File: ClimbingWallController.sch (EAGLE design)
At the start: 336 parts, among them IC1 74HCT138D, IC2 74HCT138D, IC3 PIC24FJ32GB004, IC4 SN74LV4052AD, IC5 SN74LV4052AD, IC6 TC1015, IC7 NCP1117, J1 PWR, Q1 DPBT8105, Q10 DPBT8105, Q11 DPBT8105, Q12 DPBT8105, Q13 DPBT8105, Q14 DPBT8105, Q15 DPBT8105, Q16 DPBT8105, Q17 NC, Q2 DPBT8105, Q3 DPBT8105, Q4 DPBT8105, Q5 DPBT8105, Q6 DPBT8105, Q7 DPBT8105, Q8 DPBT8105, Q9 DPBT8105, X1 MINI-USB-32005-201

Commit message: Completed routing of all circuit board elements. Created ground fills, and stitched everything together. Need to review sensitive signal coupling and review decoupling paths. Need to verify footprints.
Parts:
- added C100, C101, C99: 0.1uF, rcl:C-USC0603K
- JP1: device pinhead:PINHD-1X5/90 -> pinhead:PINHD-1X5
- XTAL1: device crystal:CRYSTALHC49UP -> Parts:CRY5032
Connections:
- removed net N$86: R85.1, R86.2
- net +5V: now also C100.1, C101.1, C99.1
- net GND: now also C100.2, C101.2, C99.2
- net TMUX0: now also IC3.AN10; no longer IC3.AN11
- net TMUX1: now also IC3.AN11; no longer IC3.AN10
- net TOUCH11: now also IC3.AN12; no longer IC5.Y0
- net TOUCH12: now also IC3.AN8; no longer IC5.Y1
- net TOUCH13: now also IC3.AN7; no longer IC5.Y2
- net TOUCH14: now also IC5.Y2; no longer IC5.Y3
- net TOUCH15: now also IC5.Y0; no longer IC5.X0
- net TOUCH16: now also IC5.Y3; no longer IC5.X1
- net TOUCH17: now also IC5.Y1; no longer IC5.X2
- net TOUCH18: now also IC5.X2; no longer IC5.X3
- net TOUCH19: now also IC5.X1; no longer IC3.AN7
- net TOUCH20: now also IC5.X0; no longer IC3.AN8
- net TOUCH21: now also IC5.X3; no longer IC3.AN12
- net VREF+: now also R85.1, R86.2

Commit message: Cleaned up floating ratsnest wires. Cleaned up DRC Errors. Need to check DRC with SEEED's rule set.
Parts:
- IC8, IC9: value TLC5952 -> (none)
- R1, R10, R100, R101, R102, R103, R104, R105, R106, R107, R108, R109, R11, R110, R111, R112, R113, R114, R115, R116, R117, R118, R119, R12, R120, R121, R122, R123, R124, R125, R126, R127, R128, R129, R13, R130, R131, R132, R133, R134, R135, R14, R15, R16, R17, R18, R19, R2, R20, R21, R22, R23, R24, R25, R26, R27, R28, R29, R3, R30, R31, R32, R33, R34, R35, R36, R37, R38, R39, R4, R40, R41, R42, R43, R44, R45, R46, R47, R48, R49, R5, R50, R51, R52, R53, R54, R57, R58, R59, R6, R60, R61, R62, R63, R64, R65, R66, R67, R68, R69, R7, R70, R71, R72, R73, R74, R75, R76, R77, R78, R79, R8, R80, R81, R82, R83, R85, R86, R87, R88, R89, R9, R90, R91, R92, R93, R94, R95, R96, R97, R98, R99: device resistor:R-US_R0603 -> Parts:R-US_R0603
- renumbered U$1 to IC8, U$2 to IC9

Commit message: DRC Passed with SEEED Rules. Added extra input to touch connector because 11-socket parts aren't available. Fixed 5v regulator pin out, and added PCB heat sink. Messed with device attributes for manufacturer part number. Exported BOM. (Awaiting clean up for BOM commit).
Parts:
- removed LED0: (no value), Parts:OSTVN12A150
- added LED4: (no value), Parts:OSTVN12A150
- C1: value 22n -> 100uF; device resistor:C-USC0603 -> resistor:CPOL-USD
- C10, C3, C4, C5, C6, C7, C8, C9: device resistor:C-USC0603 -> resistor:C-USC0603K
- C100, C101, C99: value 0.1uF -> 22n; device rcl:C-USC0603K -> resistor:C-USC0603K
- C11, C12, C13, C14: value 22n -> 0.1uF; device resistor:C-USC0603 -> rcl:C-USC0603K
- C15: value 22n -> NC; device resistor:C-USC0603 -> rcl:C-USC0603K
- C16, C90: value NC -> 0.1uF
- C17: value 0.1uF -> NC
- C18, C19, C26, C27, C28, C29, C31: value 0.1uF -> 1n; device rcl:C-USC0603K -> resistor:C-USC0603K
- C2: value 22n -> 1uF; device resistor:C-USC0603 -> rcl:C-USC0603K
- C20: value 22n -> 1n; device resistor:C-USC0603 -> resistor:C-USC0603K
- C21, C22: value NC -> 1n; device rcl:C-USC0603K -> resistor:C-USC0603K
- C23: value 470pF -> 1n; device rcl:C-USC0603K -> resistor:C-USC0603K
- C24: value 10uF -> 0.1uF; device rcl:C-USC1206K -> rcl:C-USC0603K
- C25: value 1uF -> NC
- C30, C39: value 1uF -> 1n; device rcl:C-USC0603K -> resistor:C-USC0603K
- C34: value 100uF -> 1uF; device resistor:CPOL-USD -> rcl:C-USC0603K
- C35: value 100uF -> 0.1uF; device resistor:CPOL-USD -> rcl:C-USC0603K
- C36: value 1uF -> 0.1uF
- C37: value 100uF -> NC; device resistor:CPOL-USD -> rcl:C-USC0603K
- C38: value 10uF -> 1n; device rcl:C-USC1206K -> resistor:C-USC0603K
- C40: value 100uF -> 1n; device resistor:CPOL-USD -> resistor:C-USC0603K
- C50, C51, C53, C55, C68, C70: value 1n -> NC; device resistor:C-USC0603K -> rcl:C-USC0603K
- C52, C72: value 1n -> 10uF; device resistor:C-USC0603K -> rcl:C-USC1206K
- C54, C69, C88: value 1n -> 0.1uF; device resistor:C-USC0603K -> rcl:C-USC0603K
- C71: value 1n -> 1uF; device resistor:C-USC0603K -> rcl:C-USC0603K
- C73: value 1n -> 470pF; device resistor:C-USC0603K -> rcl:C-USC0603K
- C86, C87: value 1n -> 100uF; device resistor:C-USC0603K -> resistor:CPOL-USD
- C92: value NC -> 100uF; device rcl:C-USC0603K -> resistor:CPOL-USD
- C93: value 0.1uF -> 1uF
- C94, C95, C96, C97, C98: value NC -> 22n; device rcl:C-USC0603K -> resistor:C-USC0603K
- IC2: value 74HCT138D -> SN74LV4052AD; device Parts:74HCT138D -> Parts:SN74LV4052AD
- IC4, IC5: value SN74LV4052AD -> TLC5952; device Parts:SN74LV4052AD -> Parts:TLC5952
- IC7: value NCP1117 -> (none)
- IC8: value (none) -> 74HCT138D; device Parts:TLC5952 -> Parts:74HCT138D
- IC9: value (none) -> SN74LV4052AD; device Parts:TLC5952 -> Parts:SN74LV4052AD
- J1: device con-jack:DCJ0303 -> Parts:DCJ0303
- JP1: value DEBUG -> BUZZER; device pinhead:PINHD-1X5 -> pinhead:PINHD-1X2
- JP2: value BUZZER -> DEBUG; device pinhead:PINHD-1X2 -> pinhead:PINHD-1X5
- Q17: value NC -> DPBT8105; device transistor:-NPN-SOT23-EBC -> Parts:DPBT8105
- Q9: value DPBT8105 -> NC; device Parts:DPBT8105 -> transistor:-NPN-SOT23-EBC
- R1, R13, R19, R7: value 20 -> NC
- R10, R22: value 20 -> 750
- R100, R101, R102, R103, R104, R105, R109, R110, R111, R91, R98: value 300 -> 390
- R106, R107, R108: value 300 -> 4.7k
- R112, R114, R116, R118, R124, R126, R128, R130: value 300 -> NC
- R113, R115, R117, R119, R125, R127, R129, R131: value 300 -> 20
- R12, R21, R24, R9: value NC -> 750
- R120, R121, R122, R123, R132, R133, R134, R135: value 300 -> 750
- R14, R2, R20, R8: value 750 -> 20
- R17, R5: value 750 -> NC
- R18, R6: value NC -> 20
- R25, R28, R31, R37: value 20 -> 390
- R26, R29, R32, R44: value 750 -> 390
- R27, R30, R36: value NC -> 390
- R33: value NC -> 4.7k
- R34: value 20 -> 4.7k
- R35: value 750 -> 4.7k
- R38, R41, R47: value 750 -> 300
- R39, R42, R45, R48, R85, R86, R87: value NC -> 300
- R40, R43, R46: value 20 -> 300
- R49, R50, R53, R54, R57, R58, R59, R60: value 4.7k -> 300
- R55, R56: value 1.37k 0.5% -> 300; device resistor:R-US_R0805 -> Parts:R-US_R0603
- R61, R62, R63, R64, R68, R69, R70, R71, R72, R73, R74, R75, R76, R77, R78, R79: value 390 -> 300
- R65, R66: value 390 -> 1.37k 0.5%; device Parts:R-US_R0603 -> resistor:R-US_R0805; TOLERANCE (none) -> 0.5%
- R67, R80: value 390 -> 4.7k
- R81, R83: value 390 -> NC
- R84: value 0 -> NC; device resistor:R-US_R0805 -> Parts:R-US_R0603
- R99: value 300 -> 0; device Parts:R-US_R0603 -> resistor:R-US_R0805
- TCH0, TCH1: device Parts:OSTVN11A150 -> Parts:OSTVN12A150
- X1: MPN (none) -> USB-M26FTR
- XTAL1: MPN (none) -> 7A-12.000MAAJ-T
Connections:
- removed net N$118 (its old number): C67.1, R114.1
- removed net N$66: R65.2, TCH0-4.KL
- removed net N$68: R67.2, TCH0-6.KL
- removed net N$70: R69.2, TCH0-8.KL
- removed net N$72: R71.2, TCH0-10.KL
- removed net N$74: R74.2, TCH1-2.KL
- removed net N$75: R76.2, TCH1-4.KL
- removed net N$76: R78.2, TCH1-6.KL
- removed net N$77: R80.2, TCH1-8.KL
- removed net N$78: R82.2, TCH1-10.KL
- new net N$31: R98.2, TCH0-2.KL
- new net N$32: R101.2, TCH0-4.KL
- new net N$34: C101.1, R131.1
- new net N$35: R103.2, TCH0-6.KL
- new net N$36: R105.2, TCH0-8.KL
- new net N$37: R110.2, TCH0-10.KL
- new net N$38: R26.2, TCH1-2.KL
- new net N$39: R28.2, TCH1-4.KL
- new net N$40: R30.2, TCH1-6.KL
- new net N$49: R37.2, TCH1-10.KL
- net +3V3: now also C14.1, C15.1, C25.1, C34.1, C35.1, C36.1, C37.1, C54.1, C55.1, C69.1, C70.1, C72.1, C88.1, IC2.VCC, JP2.2, R80.2, R81.2; no longer C17.1, C18.1, C19.1, C26.1, C27.1, C30.1, C31.1, C90.1, C91.1, C93.1, C94.1, C95.1, C98.1, IC8.VCC, JP1.2, R60.2, R85.2
- net +5V: now also C1.+, C11.1, C12.1, C13.1, C16.1, C17.1, C2.1, C71.1, C87.+, C90.1, C91.1, C92.+, C93.1, D10.C, D11.C, D12.C, D13.C, D14.C, D15.C, D16.C, D9.C, IC7.OUT, IC8.VCC, JP1.1, Q17.E, R1.1, R112.1, R114.1, R116.1, R118.1, R124.1, R126.1, R128.1, R13.1, R130.1, R17.1, R19.1, R5.1, R7.1, R99.2; no longer C100.1, C101.1, C25.1, C28.1, C29.1, C34.+, C36.1, C37.+, C39.1, C40.+, C96.1, C97.1, C99.1, D57.C, D58.C, D59.C, D60.C, D61.C, D62.C, D63.C, D64.C, IC2.VCC, IC7G$1.OUT, JP2.1, Q9.E, R12.1, R18.1, R21.1, R24.1, R27.1, R30.1, R33.1, R36.1, R39.1, R42.1, R45.1, R48.1, R6.1, R84.2, R9.1
- net AMSEL0: now also IC2.A, IC9.A; no longer IC4.A, IC5.A
- net AMSEL1: now also IC2.B, IC9.B; no longer IC4.B, IC5.B
- net B0: now also D17.A, IC5.OUTB0, LED2-3.KL, R47.2; no longer D19.A, IC8.OUTB0, LED0-3.KL, R90.2
- net B1: now also D20.A, IC5.OUTB1, LED2-6.KL, R50.2; no longer D22.A, IC8.OUTB1, LED0-6.KL, R93.2
- net B10: now also D23.A, IC4.OUTB2, LED1-9.KL, R55.2; no longer D49.A, IC9.OUTB2, LED2-9.KL, R120.2
- net B11: now also D26.A, IC4.OUTB3, LED1-12.KL, R58.2; no longer D52.A, IC9.OUTB3, LED2-12.KL, R123.2
- net B12: now also D35.A, IC4.OUTB4, R70.2; no longer D55.A, IC9.OUTB4, R126.2
- net B13: now also D38.A, IC4.OUTB5, R73.2; no longer D58.A, IC9.OUTB5, R129.2
- net B14: now also D47.A, IC4.OUTB6, R87.2; no longer D61.A, IC9.OUTB6, R132.2
- net B15: now also D50.A, IC4.OUTB7, R90.2; no longer D64.A, IC9.OUTB7, R135.2
- net B2: now also D29.A, IC5.OUTB2, LED2-9.KL, R61.2; no longer D25.A, IC8.OUTB2, LED0-9.KL, R96.2
- net B3: now also D32.A, IC5.OUTB3, LED2-12.KL, R64.2; no longer D28.A, IC8.OUTB3, LED0-12.KL, R99.2
- net B4: now also D41.A, IC5.OUTB4, LED4-3.KL, R76.2; no longer D31.A, IC8.OUTB4, LED1-3.KL, R102.2
- net B5: now also D44.A, IC5.OUTB5, LED4-6.KL, R79.2; no longer D34.A, IC8.OUTB5, LED1-6.KL, R105.2
- net B6: now also D53.A, IC5.OUTB6, LED4-9.KL, R94.2; no longer D37.A, IC8.OUTB6, LED1-9.KL, R108.2
- net B7: now also D56.A, IC5.OUTB7, LED4-12.KL, R97.2; no longer D40.A, IC8.OUTB7, LED1-12.KL, R111.2
- net B8: now also D11.A, IC4.OUTB0, LED1-3.KL, R40.2; no longer D43.A, IC9.OUTB0, LED2-3.KL, R114.2
- net B9: now also D14.A, IC4.OUTB1, LED1-6.KL, R43.2; no longer D46.A, IC9.OUTB1, LED2-6.KL, R117.2
- net C0_LAT: now also IC5.LAT; no longer IC8.LAT
- net C0_SCLK: now also IC5.SCLK; no longer IC8.SCLK
- net C0_SIN: now also IC5.SIN; no longer IC8.SIN
- net C0_SOUT: now also IC5.SOUT; no longer IC8.SOUT
- net C1_LAT: now also IC4.LAT; no longer IC9.LAT
- net C1_SCLK: now also IC4.SCLK; no longer IC9.SCLK
- net C1_SIN: now also IC4.SIN; no longer IC9.SIN
- net C1_SOUT: now also IC4.SOUT; no longer IC9.SOUT
- net CAIREF: now also IC5.IREF, R66.2; no longer IC8.IREF, R55.2
- net CAIREF1: now also IC4.IREF, R65.2; no longer IC9.IREF, R56.2
- net C_BLANK: now also IC4.BLANK, IC5.BLANK; no longer IC8.BLANK, IC9.BLANK
- net DISVREG: now also R67.2; no longer R59.2
- net G0: now also D16.A, IC5.OUTG0, LED2-2.KL, R46.2; no longer D18.A, IC8.OUTG0, LED0-2.KL, R89.2
- net G1: now also D19.A, IC5.OUTG1, LED2-5.KL, R49.2; no longer D21.A, IC8.OUTG1, LED0-5.KL, R92.2
- net G10: now also D22.A, IC4.OUTG2, LED1-8.KL, R54.2; no longer D48.A, IC9.OUTG2, LED2-8.KL, R119.2
- net G11: now also D25.A, IC4.OUTG3, LED1-11.KL, R57.2; no longer D51.A, IC9.OUTG3, LED2-11.KL, R122.2
- net G12: now also D34.A, IC4.OUTG4, R69.2; no longer D54.A, IC9.OUTG4, R125.2
- net G13: now also D37.A, IC4.OUTG5, R72.2; no longer D57.A, IC9.OUTG5, R128.2
- net G14: now also D46.A, IC4.OUTG6, R86.2; no longer D60.A, IC9.OUTG6, R131.2
- net G15: now also D49.A, IC4.OUTG7, R89.2; no longer D63.A, IC9.OUTG7, R134.2
- net G2: now also D28.A, IC5.OUTG2, LED2-8.KL, R60.2; no longer D24.A, IC8.OUTG2, LED0-8.KL, R95.2
- net G3: now also D31.A, IC5.OUTG3, LED2-11.KL, R63.2; no longer D27.A, IC8.OUTG3, LED0-11.KL, R98.2
- net G4: now also D40.A, IC5.OUTG4, LED4-2.KL, R75.2; no longer D30.A, IC8.OUTG4, LED1-2.KL, R101.2
- net G5: now also D43.A, IC5.OUTG5, LED4-5.KL, R78.2; no longer D33.A, IC8.OUTG5, LED1-5.KL, R104.2
- net G6: now also D52.A, IC5.OUTG6, LED4-8.KL, R93.2; no longer D36.A, IC8.OUTG6, LED1-8.KL, R107.2
- net G7: now also D55.A, IC5.OUTG7, LED4-11.KL, R96.2; no longer D39.A, IC8.OUTG7, LED1-11.KL, R110.2
- net G8: now also D10.A, IC4.OUTG0, LED1-2.KL, R39.2; no longer D42.A, IC9.OUTG0, LED2-2.KL, R113.2
- net G9: now also D13.A, IC4.OUTG1, LED1-5.KL, R42.2; no longer D45.A, IC9.OUTG1, LED2-5.KL, R116.2
- net GND: now also C1.-, C34.2, C35.2, C37.2, C40.2, C86.-, C87.-, C92.-, D57.A, D58.A, D59.A, D60.A, D61.A, D62.A, D63.A, D64.A, IC4.EPAD, IC5.EPAD, IC7.GND, JP2.3, Q9.E, R106.1, R107.1, R108.1, R33.1, R34.1, R35.1, R65.1, R66.1, R67.1, R84.1, TCH0-12.KL, TCH1-12.KL; no longer C1.2, C34.-, C35.-, C37.-, C40.-, C86.2, C87.2, C92.2, D10.A, D11.A, D12.A, D13.A, D14.A, D15.A, D16.A, D9.A, IC7G$1.GND, IC8.EPAD, IC9.EPAD, JP1.3, Q17.E, R49.1, R50.1, R51.1, R53.1, R54.1, R55.1, R56.1, R57.1, R59.1, R86.1
- net MCLR_: now also JP2.1, R82.1; no longer JP1.1, R61.1
- net N$1: now also Q13.B, R118.2, R123.2; no longer Q1.B, R2.2, R3.2
- net N$10: now also C95.1, R115.1; no longer C5.1, R13.1
- net N$100: now also C49.1, R64.1; no longer C52.1, R99.1
- net N$101: now also C62.1, R74.1; no longer C53.1, R100.1
- net N$102: now also C63.1, R75.1; no longer C54.1, R101.1
- net N$103: now also C64.1, R76.1; no longer C55.1, R102.1
- net N$104: now also C65.1, R77.1; no longer C56.1, R103.1
- net N$105: now also C66.1, R78.1; no longer C57.1, R104.1
- net N$106: now also C67.1, R79.1; no longer C58.1, R105.1
- net N$107: now also C80.1, R92.1; no longer C59.1, R106.1
- net N$108: now also C81.1, R93.1; no longer C60.1, R107.1
- net N$109: now also C82.1, R94.1; no longer C61.1, R108.1
- net N$11: now also Q10.B, R112.2, R120.2; no longer Q7.B, R17.2, R18.2
- net N$110: now also C83.1, R95.1; no longer C62.1, R109.1
- net N$111: now also C84.1, R96.1; no longer C63.1, R110.1
- net N$112: now also C85.1, R97.1; no longer C64.1, R111.1
- net N$114: now also C18.1, R38.1; no longer C65.1, R112.1
- net N$116: now also C19.1, R39.1; no longer C66.1, R113.1
- net N$12: now also C94.1, R113.1; no longer C6.1, R16.1
- net N$120: now also C21.1, R41.1; no longer C68.1, R115.1
- net N$122: now also C22.1, R42.1; no longer C69.1, R116.1
- net N$124: now also C23.1, R43.1; no longer C70.1, R117.1
- net N$126: now also C38.1, R53.1; no longer C71.1, R118.1
- net N$128: now also C39.1, R54.1; no longer C72.1, R119.1
- net N$13: now also Q14.B, R124.2, R132.2; no longer Q8.B, R20.2, R21.2
- net N$130: now also C40.1, R55.1; no longer C73.1, R120.1
- net N$132: now also C41.1, R56.1; no longer C74.1, R121.1
- net N$134: now also C42.1, R57.1; no longer C75.1, R122.1
- net N$136: now also C43.1, R58.1; no longer C76.1, R123.1
- net N$138: now also C56.1, R68.1; no longer C77.1, R124.1
- net N$14: now also C98.1, R125.1; no longer C7.1, R19.1
- net N$140: now also C57.1, R69.1; no longer C78.1, R125.1
- net N$142: now also C58.1, R70.1; no longer C79.1, R126.1
- net N$144: now also C59.1, R71.1; no longer C80.1, R127.1
- net N$146: now also C60.1, R72.1; no longer C81.1, R128.1
- net N$148: now also C61.1, R73.1; no longer C82.1, R129.1
- net N$15: now also Q8.B, R19.2; no longer Q9.B, R23.2
- net N$150: now also C74.1, R85.1; no longer C83.1, R130.1
- net N$152: now also C75.1, R86.1; no longer C84.1, R131.1
- net N$154: now also C76.1, R87.1; no longer C85.1, R132.1
- net N$156: now also C77.1, R88.1; no longer C86.1, R133.1
- net N$158: now also C78.1, R89.1; no longer C87.1, R134.1
- net N$16: now also C10.1, R20.1; no longer C8.1, R22.1
- net N$160: now also C79.1, R90.1; no longer C88.1, R135.1
- net N$17: now also Q4.B, R12.2, R7.2; no longer Q10.B, R26.2, R27.2
- net N$18: now also C6.1, R8.1; no longer C9.1, R25.1
- net N$19: now also Q3.B, R11.2, R5.2; no longer Q11.B, R29.2, R30.2
- net N$2: now also C97.1, R119.1; no longer C1.1, R1.1
- net N$20: now also C5.1, R6.1; no longer C10.1, R28.1
- net N$21: now also Q7.B, R17.2, R23.2; no longer Q12.B, R32.2, R33.2
- net N$22: now also C9.1, R18.1; no longer C11.1, R31.1
- net N$23: now also Q6.B, R15.2, R22.2; no longer Q13.B, R35.2, R36.2
- net N$24: now also C8.1, R16.1; no longer C12.1, R34.1
- net N$25: now also Q2.B, R10.2, R3.2; no longer Q14.B, R38.2, R39.2
- net N$26: now also C4.1, R4.1; no longer C13.1, R37.1
- net N$27: now also Q1.B, R1.2, R9.2; no longer Q15.B, R44.2, R45.2
- net N$28: now also C3.1, R2.1; no longer C14.1, R43.1
- net N$29: now also Q5.B, R13.2, R21.2; no longer Q16.B, R47.2, R48.2
- net N$3: now also Q12.B, R116.2, R122.2; no longer Q3.B, R5.2, R6.2
- net N$30: now also C7.1, R14.1; no longer C15.1, R46.1
- net N$33: now also Q17.B, R130.2, R135.2; no longer Q2.B, R41.2, R42.2
- net N$4: now also C96.1, R117.1; no longer C2.1, R4.1
- net N$41: now also IC8.G2A, IC8.G2B, R107.2; no longer IC1.G2A, IC1.G2B, R50.2
- net N$42: now also IC9.INH, R108.2; no longer IC4.INH, R51.2
- net N$43: now also IC1.G2A, IC1.G2B, R34.2; no longer IC2.G2A, IC2.G2B, R53.2
- net N$44: now also IC2.INH, R35.2; no longer IC5.INH, R54.2
- net N$45: now also R51.2; no longer R58.2
- net N$46: now also C68.1, R80.1, R82.2; no longer C16.1, R60.1, R61.2
- net N$47: now also R91.2; no longer R62.2
- net N$48: now also R32.2, TCH1-8.KL; no longer R63.2, TCH0-2.KL
- net N$5: now also Q16.B, R128.2, R134.2; no longer Q4.B, R8.2, R9.2
- net N$6: now also C100.1, R129.1; no longer C3.1, R7.1
- net N$65: now also R100.2; no longer R64.2
- net N$67: now also R102.2; no longer R66.2
- net N$69: now also R104.2; no longer R68.2
- net N$7: now also Q15.B, R126.2, R133.2; no longer Q5.B, R11.2, R12.2
- net N$71: now also R109.2; no longer R70.2
- net N$73: now also R111.2; no longer R72.2
- net N$79: now also R25.2; no longer R73.2
- net N$8: now also C99.1, R127.1; no longer C4.1, R10.1
- net N$80: now also R27.2; no longer R75.2
- net N$81: now also R29.2; no longer R77.2
- net N$82: now also R31.2; no longer R79.2
- net N$83: now also R36.2; no longer R81.2
- net N$84: now also R44.2; no longer R83.2
- net N$85: now also C73.1; no longer C23.1
- net N$87: now also Q9.B, R83.2; no longer Q17.B, R87.2
- net N$88: now also JP1.2, Q9.C; no longer JP2.2, Q17.C
- net N$89: now also C26.1, R45.1; no longer C41.1, R88.1
- net N$9: now also Q11.B, R114.2, R121.2; no longer Q6.B, R14.2, R15.2
- net N$90: now also C27.1, R46.1; no longer C42.1, R89.1
- net N$91: now also C28.1, R47.1; no longer C43.1, R90.1
- net N$92: now also C29.1, R48.1; no longer C44.1, R91.1
- net N$93: now also C30.1, R49.1; no longer C45.1, R92.1
- net N$94: now also C31.1, R50.1; no longer C46.1, R93.1
- net N$95: now also C44.1, R59.1; no longer C47.1, R94.1
- net N$96: now also C45.1, R60.1; no longer C48.1, R95.1
- net N$97: now also C46.1, R61.1; no longer C49.1, R96.1
- net N$98: now also C47.1, R62.1; no longer C50.1, R97.1
- net N$99: now also C48.1, R63.1; no longer C51.1, R98.1
- net OSCI: now also C50.1; no longer C22.1
- net OSCO: now also C51.1; no longer C21.1
- net PGEC: now also JP2.5; no longer JP1.5
- net PGED: now also JP2.4; no longer JP1.4
- net R0: now also D15.A, IC5.OUTR0, LED2-1.KL, R45.2; no longer D17.A, IC8.OUTR0, LED0-1.KL, R88.2
- net R1: now also D18.A, IC5.OUTR1, LED2-4.KL, R48.2; no longer D20.A, IC8.OUTR1, LED0-4.KL, R91.2
- net R10: now also D21.A, IC4.OUTR2, LED1-7.KL, R53.2; no longer D47.A, IC9.OUTR2, LED2-7.KL, R118.2
- net R11: now also D24.A, IC4.OUTR3, LED1-10.KL, R56.2; no longer D50.A, IC9.OUTR3, LED2-10.KL, R121.2
- net R12: now also D33.A, IC4.OUTR4, R68.2; no longer D53.A, IC9.OUTR4, R124.2
- net R13: now also D36.A, IC4.OUTR5, R71.2; no longer D56.A, IC9.OUTR5, R127.2
- net R14: now also D45.A, IC4.OUTR6, R85.2; no longer D59.A, IC9.OUTR6, R130.2
- net R15: now also D48.A, IC4.OUTR7, R88.2; no longer D62.A, IC9.OUTR7, R133.2
- net R2: now also D27.A, IC5.OUTR2, LED2-7.KL, R59.2; no longer D23.A, IC8.OUTR2, LED0-7.KL, R94.2
- net R3: now also D30.A, IC5.OUTR3, LED2-10.KL, R62.2; no longer D26.A, IC8.OUTR3, LED0-10.KL, R97.2
- net R4: now also D39.A, IC5.OUTR4, LED4-1.KL, R74.2; no longer D29.A, IC8.OUTR4, LED1-1.KL, R100.2
- net R5: now also D42.A, IC5.OUTR5, LED4-4.KL, R77.2; no longer D32.A, IC8.OUTR5, LED1-4.KL, R103.2
- net R6: now also D51.A, IC5.OUTR6, LED4-7.KL, R92.2; no longer D35.A, IC8.OUTR6, LED1-7.KL, R106.2
- net R7: now also D54.A, IC5.OUTR7, LED4-10.KL, R95.2; no longer D38.A, IC8.OUTR7, LED1-10.KL, R109.2
- net R8: now also D9.A, IC4.OUTR0, LED1-1.KL, R38.2; no longer D41.A, IC9.OUTR0, LED2-1.KL, R112.2
- net R9: now also D12.A, IC4.OUTR1, LED1-4.KL, R41.2; no longer D44.A, IC9.OUTR1, LED2-4.KL, R115.2
- net RAEN: now also IC8.G1, R106.2; no longer IC1.G1, R49.2
- net RBEN: now also IC1.G1, R33.2; no longer IC2.G1, R52.2
- net ROW0: now also D60.C, Q13.C, R119.2, ROW2-1.KL; no longer D1.C, Q1.C, R1.2, ROW1-1.KL
- net ROW0EN_: now also IC8.Y0, R123.1; no longer IC1.Y0, R2.1
- net ROW1: now also D64.C, Q17.C, R131.2, ROW2-2.KL; no longer D2.C, Q2.C, R40.2, ROW1-2.KL
- net ROW10: now also D3.C, Q3.C, R6.2, ROW1-3.KL; no longer D11.C, Q11.C, R28.2, ROW2-3.KL
- net ROW10EN_: now also IC1.Y2, R11.1; no longer IC2.Y2, R29.1
- net ROW11: now also D7.C, Q7.C, R18.2, ROW1-4.KL; no longer D12.C, Q12.C, R31.2, ROW2-4.KL
- net ROW11EN_: now also IC1.Y3, R23.1; no longer IC2.Y3, R32.1
- net ROW12: now also D2.C, Q2.C, R4.2, ROW1-5.KL; no longer D14.C, Q14.C, R37.2, ROW2-5.KL
- net ROW12EN_: now also IC1.Y4, R10.1; no longer IC2.Y4, R38.1
- net ROW13: now also D6.C, Q6.C, R16.2, ROW1-6.KL; no longer D13.C, Q13.C, R34.2, ROW2-6.KL
- net ROW13EN_: now also IC1.Y5, R22.1; no longer IC2.Y5, R35.1
- net ROW14: now also D1.C, Q1.C, R2.2, ROW1-7.KL; no longer D15.C, Q15.C, R43.2, ROW2-7.KL
- net ROW14EN_: now also IC1.Y6, R9.1; no longer IC2.Y6, R44.1
- net ROW15: now also D5.C, Q5.C, R14.2, ROW1-8.KL; no longer D16.C, Q16.C, R46.2, ROW2-8.KL
- net ROW15EN_: now also IC1.Y7, R21.1; no longer IC2.Y7, R47.1
- net ROW1EN_: now also IC8.Y1, R135.1; no longer IC1.Y1, R41.1
- net ROW2: now also D59.C, Q12.C, R117.2, ROW2-3.KL; no longer D3.C, Q3.C, R4.2, ROW1-3.KL
- net ROW2EN_: now also IC8.Y2, R122.1; no longer IC1.Y2, R5.1
- net ROW3: now also D63.C, Q16.C, R129.2, ROW2-4.KL; no longer D4.C, Q4.C, R7.2, ROW1-4.KL
- net ROW3EN_: now also IC8.Y3, R134.1; no longer IC1.Y3, R8.1
- net ROW4: now also D58.C, Q11.C, R115.2, ROW2-5.KL; no longer D6.C, Q6.C, R13.2, ROW1-5.KL
- net ROW4EN_: now also IC8.Y4, R121.1; no longer IC1.Y4, R14.1
- net ROW5: now also D62.C, Q15.C, R127.2, ROW2-6.KL; no longer D5.C, Q5.C, R10.2, ROW1-6.KL
- net ROW5EN_: now also IC8.Y5, R133.1; no longer IC1.Y5, R11.1
- net ROW6: now also D57.C, Q10.C, R113.2, ROW2-7.KL; no longer D7.C, Q7.C, R16.2, ROW1-7.KL
- net ROW6EN_: now also IC8.Y6, R120.1; no longer IC1.Y6, R17.1
- net ROW7: now also D61.C, Q14.C, R125.2, ROW2-8.KL; no longer D8.C, Q8.C, R19.2, ROW1-8.KL
- net ROW7EN_: now also IC8.Y7, R132.1; no longer IC1.Y7, R20.1
- net ROW8: now also D4.C, Q4.C, R8.2, ROW1-1.KL; no longer D10.C, Q10.C, R25.2, ROW2-1.KL
- net ROW8EN_: now also IC1.Y0, R12.1; no longer IC2.Y0, R26.1
- net ROW9: now also D8.C, Q8.C, R20.2, ROW1-2.KL; no longer D9.C, Q9.C, R22.2, ROW2-2.KL
- net ROW9EN_: now also IC1.Y1, R24.1; no longer IC2.Y1, R23.1
- net RSEL0: now also IC8.A; no longer IC2.A
- net RSEL1: now also IC8.B; no longer IC2.B
- net RSEL2: now also IC8.C; no longer IC2.C
- net TMUX0: now also IC9.Y; no longer IC4.Y
- net TMUX1: now also IC9.X; no longer IC4.X
- net TMUX2: now also IC2.Y; no longer IC5.Y
- net TMUX3: now also IC2.X; no longer IC5.X
- net TOUCH0: now also R91.1; no longer R62.1
- net TOUCH1: now also R98.1; no longer R63.1
- net TOUCH10: now also IC9.X3, R111.1; no longer IC4.X3, R72.1
- net TOUCH11: now also R25.1; no longer R73.1
- net TOUCH12: now also R26.1; no longer R74.1
- net TOUCH13: now also R27.1; no longer R75.1
- net TOUCH14: now also IC2.Y2, R28.1; no longer IC5.Y2, R76.1
- net TOUCH15: now also IC2.Y0, R29.1; no longer IC5.Y0, R77.1
- net TOUCH16: now also IC2.Y3, R30.1; no longer IC5.Y3, R78.1
- net TOUCH17: now also IC2.Y1, R31.1; no longer IC5.Y1, R79.1
- net TOUCH18: now also IC2.X2, R32.1; no longer IC5.X2, R80.1
- net TOUCH19: now also IC2.X1, R36.1; no longer IC5.X1, R81.1
- net TOUCH2: now also R100.1; no longer R64.1
- net TOUCH20: now also IC2.X0, R37.1; no longer IC5.X0, R82.1
- net TOUCH21: now also IC2.X3, R44.1; no longer IC5.X3, R83.1
- net TOUCH3: now also IC9.Y2, R101.1; no longer IC4.Y2, R65.1
- net TOUCH4: now also IC9.Y0, R102.1; no longer IC4.Y0, R66.1
- net TOUCH5: now also IC9.Y3, R103.1; no longer IC4.Y3, R67.1
- net TOUCH6: now also IC9.Y1, R104.1; no longer IC4.Y1, R68.1
- net TOUCH7: now also IC9.X2, R105.1; no longer IC4.X2, R69.1
- net TOUCH8: now also IC9.X1, R109.1; no longer IC4.X1, R70.1
- net TOUCH9: now also IC9.X0, R110.1; no longer IC4.X0, R71.1
- net V+: now also C86.+, IC7.IN, R99.1; no longer C35.+, IC7G$1.IN, R84.1
- net VBUS: now also R51.1, R52.2; no longer R57.2, R58.1
- net VDDCORE: now also C52.1, C53.1; no longer C38.1, C92.1
- net VREF+: now also R81.1, R83.1, R84.2; no longer R85.1, R86.2, R87.1
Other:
- moved on the sheet: C10, C100, C101, C11, C12, C13, C14, C15, C16, C17, C18, C19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

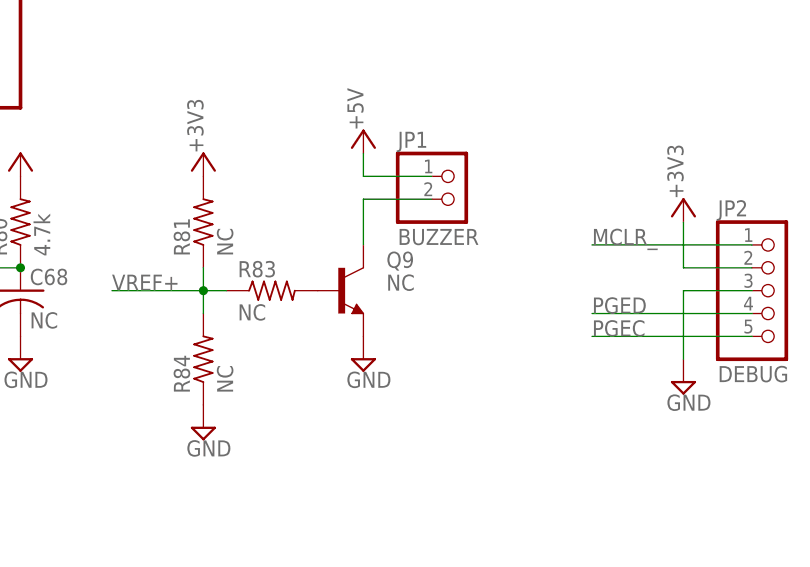
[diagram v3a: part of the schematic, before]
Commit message: Increased LED Driver power pad to recommended specs. Exported BOM, massaged, and identified parts at digikey.csv. Setup a Digikey BOM.
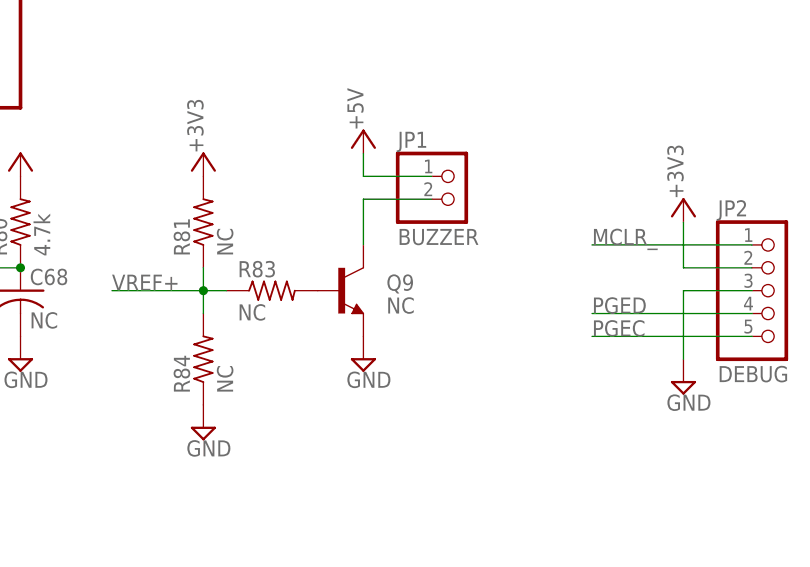
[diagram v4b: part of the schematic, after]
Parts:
- Q9: device transistor:-NPN-SOT23-EBC -> transistor:BC847A-NPN-SOT23-BEC
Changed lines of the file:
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@@
 <part name="+3V15" library="supply1" deviceset="+3V3" device=""/>
 <part name="SUPPLY69" library="supply2" deviceset="GND" device=""/>
-<part name="Q9" library="transistor" deviceset="*-NPN-" device="SOT23-EBC" value="NC"/>
 <part name="R83" library="Parts" deviceset="R-US_" device="R0603" value="NC"/>
 <part name="SUPPLY70" library="supply2" deviceset="GND" device=""/>
@@
 <part name="SUPPLY147" library="supply2" deviceset="GND" device=""/>
 <part name="IC7" library="Parts" deviceset="NCP1117" device=""/>
+<part name="Q9" library="transistor" deviceset="*-NPN-" device="SOT23-BEC" technology="BC847A" value="NC"/>
 </parts>
 <sheets>
@@
 </instance>
 <instance part="SUPPLY69" gate="GND" x="-403.86" y="93.98"/>
-<instance part="Q9" gate="G$1" x="-388.62" y="109.22" smashed="yes">
-<attribute name="NAME" x="-383.54" y="111.76" size="1.778" layer="95"/>
-<attribute name="VALUE" x="-383.54" y="109.22" size="1.778" layer="96"/>
-</instance>
 <instance part="R83" gate="G$1" x="-396.24" y="109.22"/>
 <instance part="SUPPLY70" gate="GND" x="-386.08" y="101.6"/>
@@
 <instance part="SUPPLY147" gate="GND" x="-332.74" y="223.52"/>
 <instance part="IC7" gate="G$1" x="-561.34" y="45.72"/>
+<instance part="Q9" gate="G$1" x="-388.62" y="109.22" smashed="yes">
+<attribute name="NAME" x="-383.54" y="109.22" size="1.778" layer="95"/>
+<attribute name="VALUE" x="-383.54" y="106.68" size="1.778" layer="96"/>
+</instance>
 </instances>
 <busses>
@@
 </segment>
 <segment>
-<pinref part="Q9" gate="G$1" pin="E"/>
-<pinref part="SUPPLY70" gate="GND" pin="GND"/>
-</segment>
-<segment>
 <pinref part="SUPPLY71" gate="GND" pin="GND"/>
 <pinref part="C14" gate="G$1" pin="2"/>
@@
 <pinref part="IC7" gate="G$1" pin="GND"/>
 </segment>
+<segment>
+<pinref part="SUPPLY70" gate="GND" pin="GND"/>
+<pinref part="Q9" gate="G$1" pin="E"/>
+</segment>
 </net>
 <net name="ROW0EN_" class="0">
@@
 </segment>
 </net>
-<net name="N$87" class="0">
-<segment>
-<pinref part="Q9" gate="G$1" pin="B"/>
-<pinref part="R83" gate="G$1" pin="2"/>
-</segment>
-</net>
 <net name="N$88" class="0">
 <segment>
-<pinref part="Q9" gate="G$1" pin="C"/>
 <pinref part="JP1" gate="G$1" pin="2"/>
 <wire x1="-378.46" y1="119.38" x2="-386.08" y2="119.38" width="0.1524" layer="91"/>
 <wire x1="-386.08" y1="119.38" x2="-386.08" y2="114.3" width="0.1524" layer="91"/>
+<pinref part="Q9" gate="G$1" pin="C"/>
 </segment>
 </net>
@@
 </segment>
 </net>
+<net name="N$50" class="0">
+<segment>
+<pinref part="R83" gate="G$1" pin="2"/>
+<pinref part="Q9" gate="G$1" pin="B"/>
+</segment>
+</net>

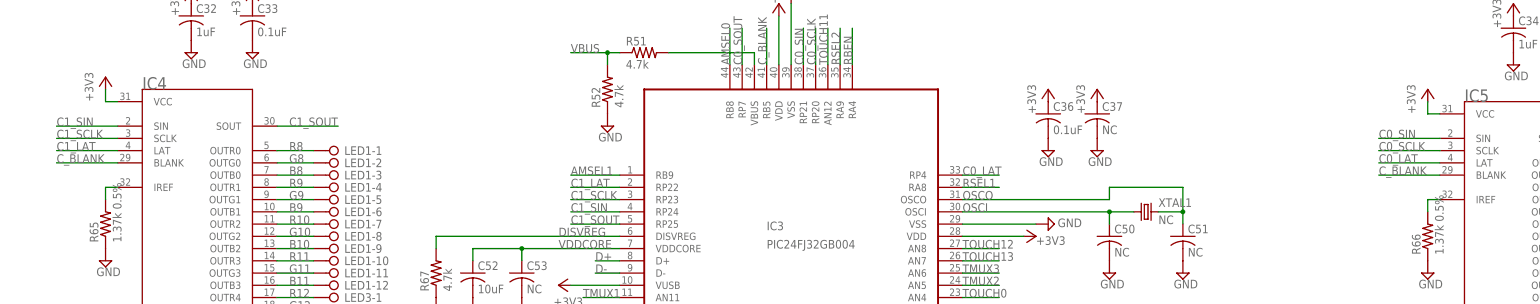
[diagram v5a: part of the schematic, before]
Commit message: Added Logos to board. Cleaned up part names on board. Fixed LED driver part name.
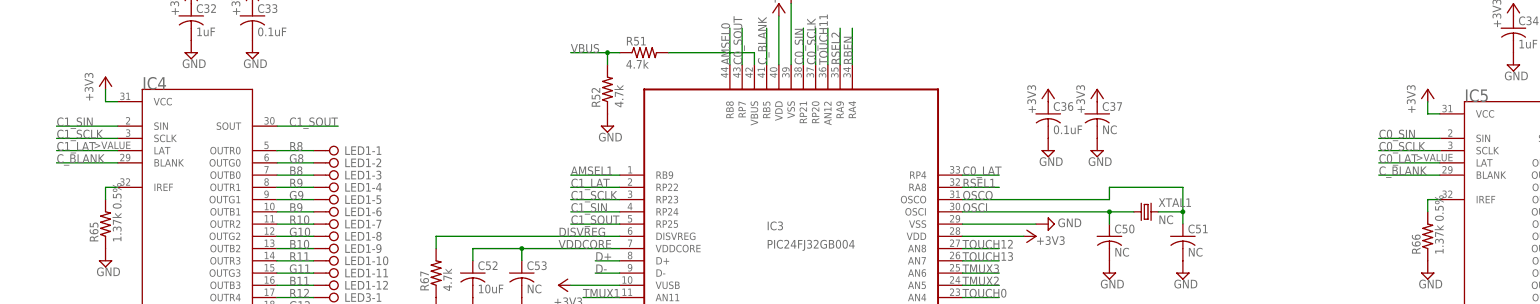
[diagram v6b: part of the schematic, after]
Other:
- moved on the sheet: IC4, IC5

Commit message: Updated NC status on column clamp diodes. Added new datasheet.
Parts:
- C11, C12, C13: value 0.1uF -> NC
- D10, D11, D12, D13, D14, D15, D16, D17, D18, D19, D20, D21, D22, D23, D24, D25, D26, D27, D28, D29, D30, D31, D32, D33, D34, D35, D36, D37, D38, D39, D40, D41, D42, D43, D44, D45, D46, D47, D48, D49, D50, D51, D52, D53, D54, D55, D56, D9: value RB521S30T1G -> NC
